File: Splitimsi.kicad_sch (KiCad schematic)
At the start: 45 parts, among them SW1 MX_RGB, SW10 MX_RGB, SW11 MX_RGB, SW12 RotaryEncoder_Switch, SW13 MX_RGB, SW14 MX_RGB, SW15 MX_RGB, SW16 MX_RGB, SW17 MX_RGB, SW18 MX_RGB, SW19 MX_RGB, SW2 MX_RGB, SW20 MX_RGB, SW21 MX_RGB, SW22 MX_RGB, SW23 MX_RGB, SW24 MX_RGB, SW25 MX_RGB, SW26 MX_RGB, SW27 MX_RGB, SW28 MX_RGB, SW29 MX_RGB, SW3 MX_RGB, SW30 MX_RGB, SW4 MX_RGB, SW5 MX_RGB, SW6 RotaryEncoder_Switch, SW7 MX_RGB, SW8 MX_RGB, SW9 MX_RGB, U2 TRRS

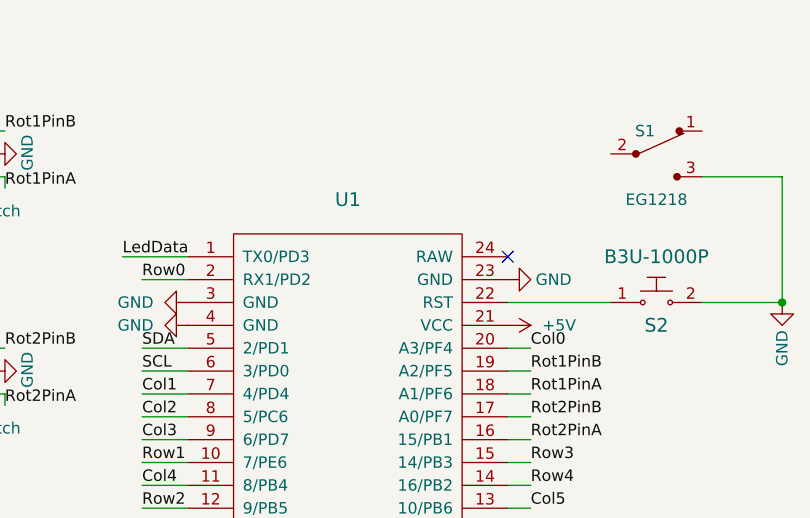
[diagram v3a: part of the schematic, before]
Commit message: battery pins added to the schematic and pcb
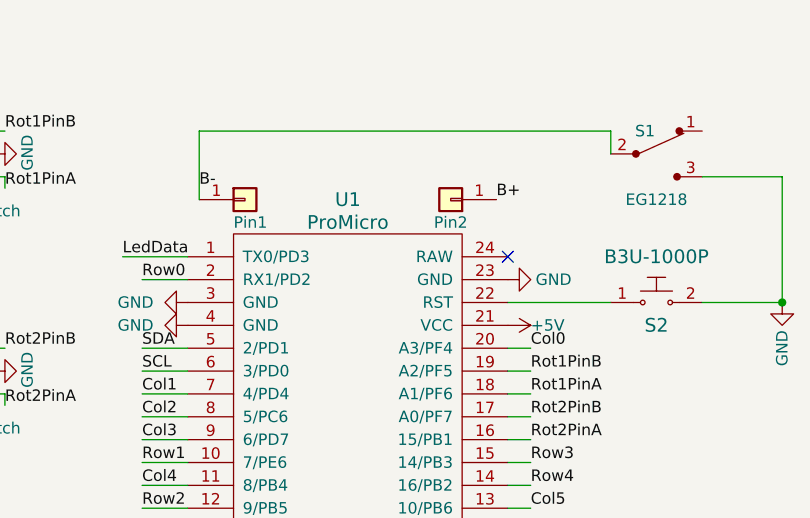
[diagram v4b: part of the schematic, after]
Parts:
- added Pin1: (no value), symbol Connector_Generic:Conn_01x01
- added Pin2: Conn_01x01, Keebio-Parts:SinglePad, symbol Connector_Generic:Conn_01x01
- U1: value (none) -> ProMicro; footprint (none) -> Keebio-Parts:ArduinoProMicro
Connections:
- net B-: now reaches S1.2
- net B-: now also Pin1.1 (Pin_1)
- new net B+: Pin2.1 (Pin_1)
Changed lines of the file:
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@@
     (stroke (width 0) (type default) (color 0 0 0 0))
   )
+  (wire (pts (xy 151.13 25.4) (xy 196.85 25.4))
+    (stroke (width 0) (type default) (color 0 0 0 0))
+  )
   (wire (pts (xy 91.44 49.53) (xy 91.44 52.07))
     (stroke (width 0) (type default) (color 0 0 0 0))
@@
     (stroke (width 0) (type default) (color 0 0 0 0))
   )
+  (wire (pts (xy 151.13 33.02) (xy 151.13 25.4))
+    (stroke (width 0) (type default) (color 0 0 0 0))
+  )
   (wire (pts (xy 55.88 54.61) (xy 62.23 54.61))
     (stroke (width 0) (type default) (color 0 0 0 0))
@@
     (stroke (width 0) (type default) (color 0 0 0 0))
   )
+  (wire (pts (xy 196.85 25.4) (xy 196.85 27.94))
+    (stroke (width 0) (type default) (color 0 0 0 0))
+  )
   (wire (pts (xy 45.72 15.24) (xy 45.72 22.86))
     (stroke (width 0) (type default) (color 0 0 0 0))
@@
     (effects (font (size 1.27 1.27)) (justify left bottom))
   )
+  (label "B-" (at 151.13 31.75 0)
+    (effects (font (size 1.27 1.27)) (justify left bottom))
+  )
   (label "Col3" (at 73.66 15.24 0)
     (effects (font (size 1.27 1.27)) (justify left bottom))
@@
     (effects (font (size 1.27 1.27)) (justify left bottom))
   )
+  (label "B+" (at 184.15 33.02 0)
+    (effects (font (size 1.27 1.27)) (justify left bottom))
+  )
   (label "Col1" (at 144.78 54.61 0)
     (effects (font (size 1.27 1.27)) (justify left bottom))
@@
     (pin "1")
   )
+  (symbol (lib_id "Connector_Generic:Conn_01x01") (at 156.21 33.02 0) (unit 1)
+    (in_bom yes) (on_board yes)
+    (property "Reference" "Pin1" (id 0) (at 154.94 35.56 0)
+      (effects (font (size 1.27 1.27)) (justify left))
+    )
+    (property "Value" "" (id 1) (at 151.13 29.21 0)
+      (effects (font (size 1.27 1.27)) (justify left) hide)
+    )
+    (property "Footprint" "" (id 2) (at 156.21 33.02 0)
+      (effects (font (size 1.27 1.27)) hide)
+    )
+    (property "Datasheet" "~" (id 3) (at 156.21 33.02 0)
+      (effects (font (size 1.27 1.27)) hide)
+    )
+    (pin "1")
+  )
   (symbol (lib_id "power:+5V") (at 77.47 109.22 180) (unit 1)
     (in_bom yes) (on_board yes)
@@
     (pin "1")
   )
+  (symbol (lib_id "Connector_Generic:Conn_01x01") (at 179.07 33.02 180) (unit 1)
+    (in_bom yes) (on_board yes)
+    (property "Reference" "Pin2" (id 0) (at 179.07 35.56 0))
+    (property "Value" "Conn_01x01" (id 1) (at 179.07 29.21 0)
+      (effects (font (size 1.27 1.27)) hide)
+    )
+    (property "Footprint" "Keebio-Parts:SinglePad" (id 2) (at 179.07 33.02 0)
+      (effects (font (size 1.27 1.27)) hide)
+    )
+    (property "Datasheet" "~" (id 3) (at 179.07 33.02 0)
+      (effects (font (size 1.27 1.27)) hide)
+    )
+    (pin "1")
+  )
   (symbol (lib_name "MX_RGB_23") (lib_id "KeyboardCustomSym:MX_RGB") (at 93.98 97.79 0) (unit 1)
     (in_bom yes) (on_board yes) (fields_autoplaced)
@@
   (symbol (lib_id "power:PWR_FLAG") (at 160.02 80.01 0) (unit 1)
     (in_bom yes) (on_board yes) (fields_autoplaced)
-    (property "Reference" "#FLG?" (id 0) (at 160.02 78.105 0)
+    (property "Reference" "#FLG01" (id 0) (at 160.02 78.105 0)
       (effects (font (size 1.27 1.27)) hide)
     )
@@
   (symbol (lib_id "power:PWR_FLAG") (at 175.26 92.71 270) (unit 1)
     (in_bom yes) (on_board yes)
-    (property "Reference" "#FLG?" (id 0) (at 177.165 92.71 0)
+    (property "Reference" "#FLG02" (id 0) (at 177.165 92.71 0)
       (effects (font (size 1.27 1.27)) hide)
     )
@@
   )
   (symbol (lib_id "power:+5V") (at 185.42 46.99 270) (unit 1)
-    (in_bom yes) (on_board yes) (fields_autoplaced)
+    (in_bom yes) (on_board yes)
     (property "Reference" "#PWR016" (id 0) (at 181.61 46.99 0)
       (effects (font (size 1.27 1.27)) hide)
     )
-    (property "Value" "+5V" (id 1) (at 189.23 46.9899 90)
+    (property "Value" "+5V" (id 1) (at 187.96 46.99 90)
       (effects (font (size 1.27 1.27)) (justify left))
     )
@@
       (effects (font (size 1.524 1.524)))
     )
-    (property "Value" "" (id 1) (at 167.64 35.56 0)
+    (property "Value" "ProMicro" (id 1) (at 167.64 35.56 0)
       (effects (font (size 1.524 1.524)))
     )
-    (property "Footprint" "" (id 2) (at 194.31 116.84 90)
+    (property "Footprint" "Keebio-Parts:ArduinoProMicro" (id 2) (at 194.31 116.84 90)
       (effects (font (size 1.524 1.524)) hide)
     )
@@
   (symbol_instances
     (path "/9eba5d0f-5c14-4f7a-816d-ad5683ef7504"
-      (reference "#FLG?") (unit 1) (value "PWR_FLAG") (footprint "")
+      (reference "#FLG01") (unit 1) (value "PWR_FLAG") (footprint "")
     )
     (path "/c8f07988-6923-43c1-86bc-6009e69a36e7"
-      (reference "#FLG?") (unit 1) (value "PWR_FLAG") (footprint "")
+      (reference "#FLG02") (unit 1) (value "PWR_FLAG") (footprint "")
     )
     (path "/44b5dc72-4ec6-4fb2-b842-6217e1e756c0"
@@
       (reference "H6") (unit 1) (value "Hole") (footprint "aio3-misc:Generic-Mounthole")
     )
+    (path "/4e8b8c7b-3494-4b98-94fc-b24608211867"
+      (reference "Pin1") (unit 1) (value "Conn_01x01") (footprint "Keebio-Parts:SinglePad")
+    )
+    (path "/978b5aff-ce0d-4c9c-a9f7-3c3fa0a5a3a1"
+      (reference "Pin2") (unit 1) (value "Conn_01x01") (footprint "Keebio-Parts:SinglePad")
+    )
     (path "/51436f05-58a2-480a-b19d-fa9db125d54d"

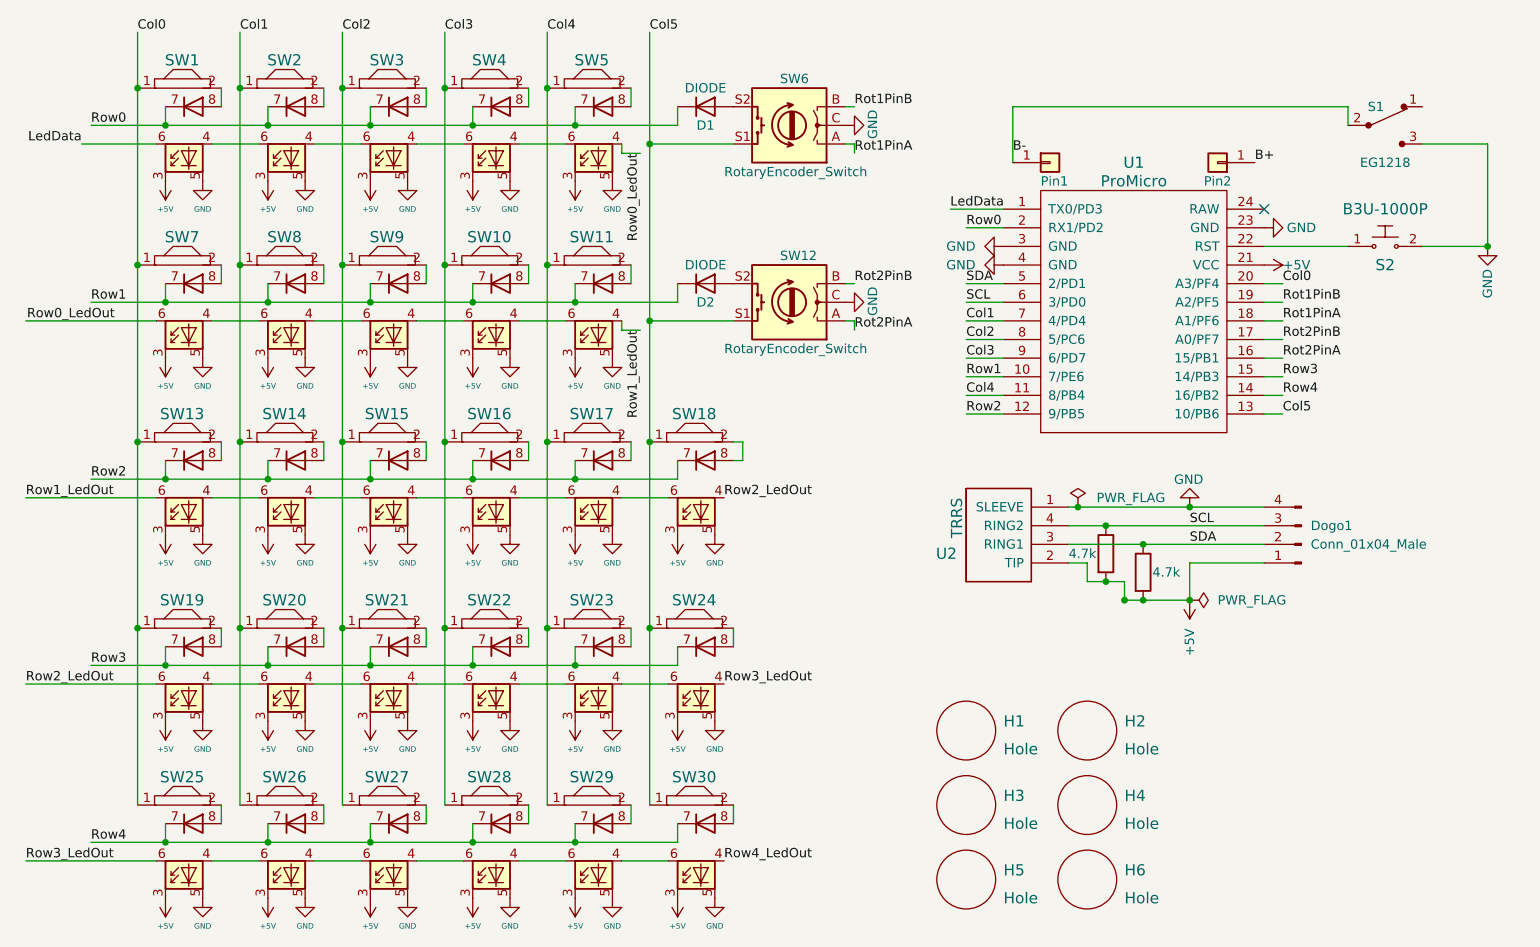
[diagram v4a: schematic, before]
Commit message: Power flags added for battery and led powers connected to the battery
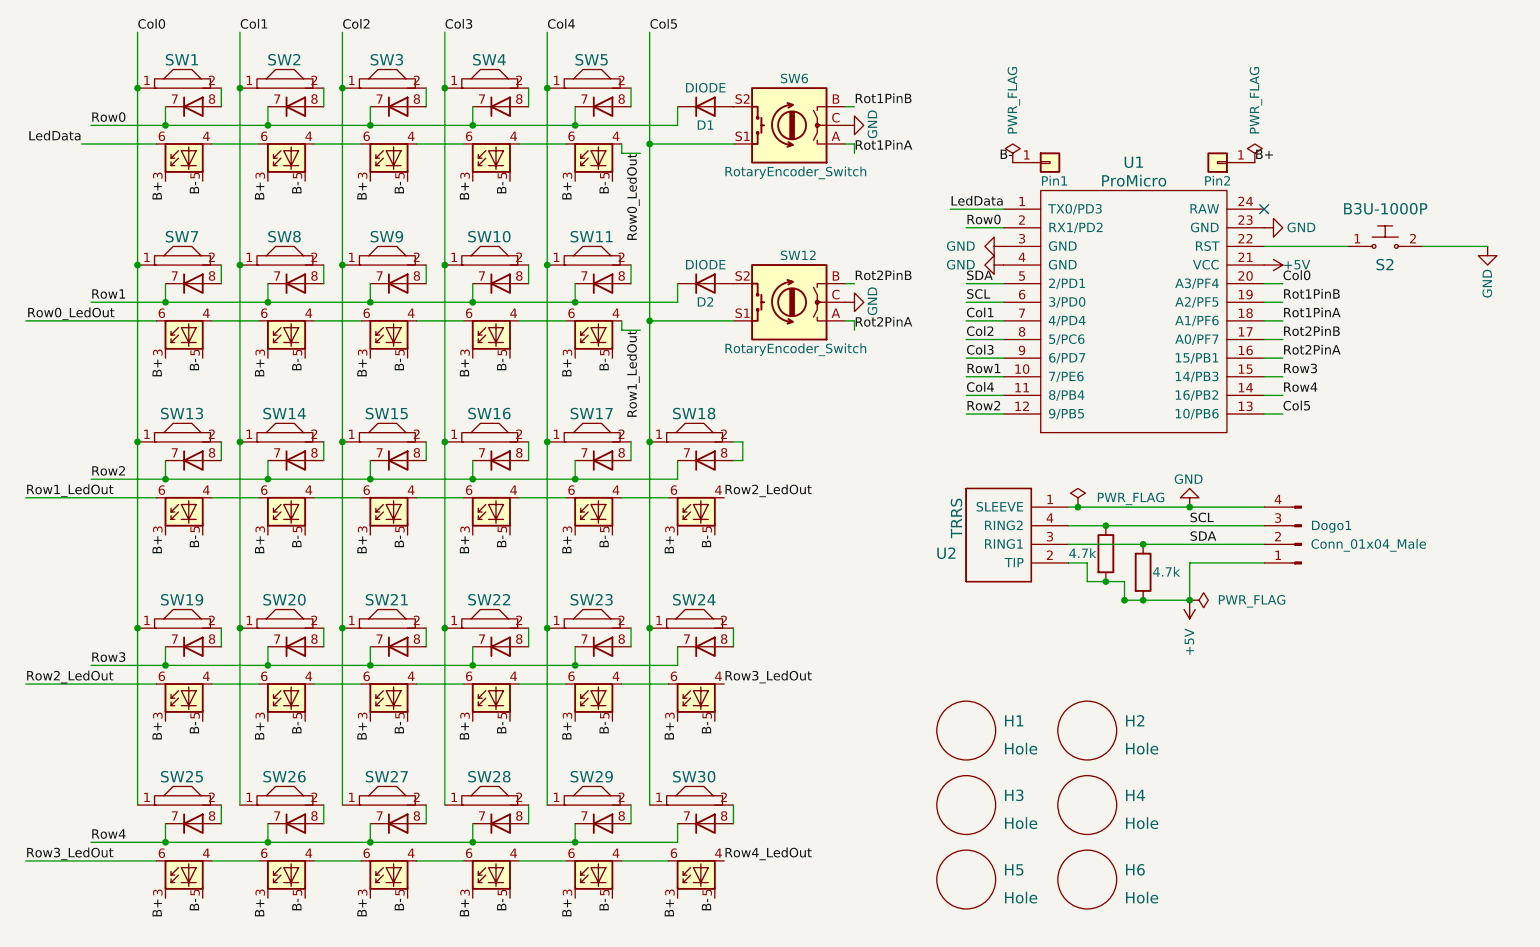
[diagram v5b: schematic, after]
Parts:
- removed S1: EG1218, digikey-footprints:Switch_Slide_11.6x4mm_EG1218, symbol dk_Slide-Switches:EG1218
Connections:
- net +5V: no longer SW1.3 (VDD), SW10.3 (VDD), SW11.3 (VDD), SW13.3 (VDD), SW14.3 (VDD), SW15.3 (VDD), SW16.3 (VDD), SW17.3 (VDD), SW18.3 (VDD), SW19.3 (VDD), SW2.3 (VDD), SW20.3 (VDD), SW21.3 (VDD), SW22.3 (VDD), SW23.3 (VDD), SW24.3 (VDD), SW25.3 (VDD), SW26.3 (VDD), SW27.3 (VDD), SW28.3 (VDD), SW29.3 (VDD), SW3.3 (VDD), SW30.3 (VDD), SW4.3 (VDD), SW5.3 (VDD), SW7.3 (VDD), SW8.3 (VDD), SW9.3 (VDD)
- net B+: now also SW1.3 (VDD), SW10.3 (VDD), SW11.3 (VDD), SW13.3 (VDD), SW14.3 (VDD), SW15.3 (VDD), SW16.3 (VDD), SW17.3 (VDD), SW18.3 (VDD), SW19.3 (VDD), SW2.3 (VDD), SW20.3 (VDD), SW21.3 (VDD), SW22.3 (VDD), SW23.3 (VDD), SW24.3 (VDD), SW25.3 (VDD), SW26.3 (VDD), SW27.3 (VDD), SW28.3 (VDD), SW29.3 (VDD), SW3.3 (VDD), SW30.3 (VDD), SW4.3 (VDD), SW5.3 (VDD), SW7.3 (VDD), SW8.3 (VDD), SW9.3 (VDD)
- net B-: now also SW1.5 (GND), SW10.5 (GND), SW11.5 (GND), SW13.5 (GND), SW14.5 (GND), SW15.5 (GND), SW16.5 (GND), SW17.5 (GND), SW18.5 (GND), SW19.5 (GND), SW2.5 (GND), SW20.5 (GND), SW21.5 (GND), SW22.5 (GND), SW23.5 (GND), SW24.5 (GND), SW25.5 (GND), SW26.5 (GND), SW27.5 (GND), SW28.5 (GND), SW29.5 (GND), SW3.5 (GND), SW30.5 (GND), SW4.5 (GND), SW5.5 (GND), SW7.5 (GND), SW8.5 (GND), SW9.5 (GND)
- net GND: no longer SW1.5 (GND), SW10.5 (GND), SW11.5 (GND), SW13.5 (GND), SW14.5 (GND), SW15.5 (GND), SW16.5 (GND), SW17.5 (GND), SW18.5 (GND), SW19.5 (GND), SW2.5 (GND), SW20.5 (GND), SW21.5 (GND), SW22.5 (GND), SW23.5 (GND), SW24.5 (GND), SW25.5 (GND), SW26.5 (GND), SW27.5 (GND), SW28.5 (GND), SW29.5 (GND), SW3.5 (GND), SW30.5 (GND), SW4.5 (GND), SW5.5 (GND), SW7.5 (GND), SW8.5 (GND), SW9.5 (GND)

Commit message: MCU adjusted on pcb
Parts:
- Pin1: value (none) -> Conn_01x01; footprint (none) -> Keebio-Parts:SinglePad
- SW18: value MX_RGB -> (none); footprint KeyboardCustomFPs:Kailh_HS_MX_LED -> (none)
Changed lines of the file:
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@@
       (effects (font (size 1.524 1.524)))
     )
-    (property "Value" "MX_RGB" (id 1) (at 107.7276 67.3151 0)
-      (effects (font (size 1.524 1.524)) hide)
-    )
-    (property "Footprint" "KeyboardCustomFPs:Kailh_HS_MX_LED" (id 2) (at 106.5571 64.655 0)
+    (property "Value" "" (id 1) (at 107.7276 67.3151 0)
+      (effects (font (size 1.524 1.524)) hide)
+    )
+    (property "Footprint" "" (id 2) (at 106.5571 64.655 0)
       (effects (font (size 1.524 1.524)) hide)
     )
@@
       (effects (font (size 1.27 1.27)) (justify left))
     )
-    (property "Value" "" (id 1) (at 151.13 29.21 0)
+    (property "Value" "Conn_01x01" (id 1) (at 151.13 29.21 0)
       (effects (font (size 1.27 1.27)) (justify left) hide)
     )
-    (property "Footprint" "" (id 2) (at 156.21 33.02 0)
+    (property "Footprint" "Keebio-Parts:SinglePad" (id 2) (at 156.21 33.02 0)
       (effects (font (size 1.27 1.27)) hide)
     )
@@
     )
     (path "/26d58434-7bc0-4330-aacc-ebafc1af4dff"
-      (reference "SW18") (unit 1) (value "MX_RGB") (footprint "KeyboardCustomFPs:Kailh_HS_MX_LED")
+      (reference "SW18") (unit 1) (value "MX_RGB") (footprint "KeyboardCustomFPs:Kailh_HS_MX_LED_option2")
     )
     (path "/0cb1d01e-f5f0-4c79-8ca3-b02247355dc9"

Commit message: Common ground zone fill for both sides
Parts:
- SW18: value (none) -> MX_RGB; footprint (none) -> KeyboardCustomFPs:Kailh_HS_MX_LED_option2
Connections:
- net B- is gone; now on net GND: Pin1.1 (Pin_1), SW1.5 (GND), SW10.5 (GND), SW11.5 (GND), SW13.5 (GND), SW14.5 (GND), SW15.5 (GND), SW16.5 (GND), SW17.5 (GND), SW18.5 (GND), SW19.5 (GND), SW2.5 (GND), SW20.5 (GND), SW21.5 (GND), SW22.5 (GND), SW23.5 (GND), SW24.5 (GND), SW25.5 (GND), SW26.5 (GND), SW27.5 (GND), SW28.5 (GND), SW29.5 (GND), SW3.5 (GND), SW30.5 (GND), SW4.5 (GND), SW5.5 (GND), SW7.5 (GND), SW8.5 (GND), SW9.5 (GND)
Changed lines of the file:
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@@
+    (effects (font (size 1.27 1.27)) (justify right bottom))
+  )
+  (label "B-" (at 203.2 25.4 180)
     (effects (font (size 1.27 1.27)) (justify right bottom))
   )
@@
       (effects (font (size 1.524 1.524)))
     )
-    (property "Value" "" (id 1) (at 107.7276 67.3151 0)
-      (effects (font (size 1.524 1.524)) hide)
-    )
-    (property "Footprint" "" (id 2) (at 106.5571 64.655 0)
+    (property "Value" "MX_RGB" (id 1) (at 107.7276 67.3151 0)
+      (effects (font (size 1.524 1.524)) hide)
+    )
+    (property "Footprint" "KeyboardCustomFPs:Kailh_HS_MX_LED_option2" (id 2) (at 106.5571 64.655 0)
       (effects (font (size 1.524 1.524)) hide)
     )
@@
   (symbol (lib_id "power:PWR_FLAG") (at 184.15 33.02 0) (unit 1)
     (in_bom yes) (on_board yes)
-    (property "Reference" "#FLG?" (id 0) (at 184.15 31.115 0)
+    (property "Reference" "#FLG0102" (id 0) (at 184.15 31.115 0)
       (effects (font (size 1.27 1.27)) hide)
     )
@@
   (symbol (lib_id "power:PWR_FLAG") (at 151.13 33.02 0) (unit 1)
     (in_bom yes) (on_board yes)
-    (property "Reference" "#FLG?" (id 0) (at 151.13 31.115 0)
+    (property "Reference" "#FLG0101" (id 0) (at 151.13 31.115 0)
       (effects (font (size 1.27 1.27)) hide)
     )
@@
     )
     (property "Datasheet" "~" (id 3) (at 160.02 80.01 0)
+      (effects (font (size 1.27 1.27)) hide)
+    )
+    (pin "1")
+  )
+  (symbol (lib_id "power:GND") (at 203.2 25.4 0) (unit 1)
+    (in_bom yes) (on_board yes) (fields_autoplaced)
+    (property "Reference" "#PWR0101" (id 0) (at 203.2 31.75 0)
+      (effects (font (size 1.27 1.27)) hide)
+    )
+    (property "Value" "GND" (id 1) (at 203.2 30.48 0))
+    (property "Footprint" "" (id 2) (at 203.2 25.4 0)
+      (effects (font (size 1.27 1.27)) hide)
+    )
+    (property "Datasheet" "" (id 3) (at 203.2 25.4 0)
       (effects (font (size 1.27 1.27)) hide)
     )
@@
       (reference "#FLG02") (unit 1) (value "PWR_FLAG") (footprint "")
     )
+    (path "/90d63027-85ae-40ec-bf42-cad9b49b8942"
+      (reference "#FLG0101") (unit 1) (value "PWR_FLAG") (footprint "")
+    )
     (path "/4058e830-cb43-4d30-9bb9-06a51898acd1"
-      (reference "#FLG?") (unit 1) (value "PWR_FLAG") (footprint "")
-    )
-    (path "/90d63027-85ae-40ec-bf42-cad9b49b8942"
-      (reference "#FLG?") (unit 1) (value "PWR_FLAG") (footprint "")
+      (reference "#FLG0102") (unit 1) (value "PWR_FLAG") (footprint "")
     )
     (path "/44b5dc72-4ec6-4fb2-b842-6217e1e756c0"
@@
       (reference "#PWR041") (unit 1) (value "+5V") (footprint "")
     )
+    (path "/a59bd763-2144-4f0b-809d-d637e0dfcdc4"
+      (reference "#PWR0101") (unit 1) (value "GND") (footprint "")
+    )
     (path "/cefa7dfe-2569-4624-baca-5c5512c57761"

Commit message: MCU silkscreen simplified
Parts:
- Dogo1: value Conn_01x04_Male -> (none); footprint Connector_PinSocket_2.00mm:PinSocket_1x04_P2.00mm_Vertical -> (none)
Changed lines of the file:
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@@
     (in_bom yes) (on_board yes) (fields_autoplaced)
     (property "Reference" "Dogo1" (id 0) (at 191.77 82.5499 0)
+      (effects (font (size 1.27 1.27)) (justify right) hide)
+    )
+    (property "Value" "" (id 1) (at 191.77 83.8199 0)
       (effects (font (size 1.27 1.27)) (justify right))
     )
-    (property "Value" "Conn_01x04_Male" (id 1) (at 191.77 85.0899 0)
-      (effects (font (size 1.27 1.27)) (justify right))
-    )
-    (property "Footprint" "Connector_PinSocket_2.00mm:PinSocket_1x04_P2.00mm_Vertical" (id 2) (at 190.5 85.09 0)
+    (property "Footprint" "" (id 2) (at 190.5 85.09 0)
       (effects (font (size 1.27 1.27)) hide)
     )
